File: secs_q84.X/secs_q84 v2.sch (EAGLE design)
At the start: 51 parts, among them IC1 MAX203ECWP, IC4 PIC18F47Q84-I_PT

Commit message: u[p
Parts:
- added SV2: CANBUS, con-lstb:MA06-1
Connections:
- net PVP_A renamed RS232_TX_OUT
- removed net PVP_B: A+REV.1, B-NORM.1, PVP_0.7
- new net RS232_RX_IN: A+REV.1, B-NORM.1, PVP_0.4
- net CANRX: now also SV2.2
- net CANTX: now also SV2.3
- net DERE: now also SV2.4
- net VCC: now also C2.1
- net VDD: now also SV2.5; no longer C2.1
- net VSS: now also SV2.1
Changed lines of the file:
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@@
 <part name="R1" library="rcl" library_urn="urn:adsk.eagle:library:334" deviceset="R-US_" device="R0805" package3d_urn="urn:adsk.eagle:package:23553/2" value="0ohm"/>
 <part name="VDD8" library="supply1" library_urn="urn:adsk.eagle:library:371" deviceset="VDD" device=""/>
+<part name="SV2" library="con-lstb" library_urn="urn:adsk.eagle:library:162" deviceset="MA06-1" device="" package3d_urn="urn:adsk.eagle:package:8340/1" value="CANBUS"/>
+<part name="P+4" library="supply1" library_urn="urn:adsk.eagle:library:371" deviceset="VCC" device=""/>
 </parts>
 <sheets>
@@
 </plain>
 <instances>
-<instance part="VDD1" gate="G$1" x="93.98" y="0" smashed="yes">
-<attribute name="VALUE" x="101.6" y="0" size="1.778" layer="96" rot="R180"/>
+<instance part="VDD1" gate="G$1" x="99.06" y="0" smashed="yes">
+<attribute name="VALUE" x="106.68" y="0" size="1.778" layer="96" rot="R180"/>
 </instance>
 <instance part="OS1_10MHZ" gate="A" x="134.62" y="-27.94" smashed="yes">
@@
 <attribute name="VALUE" x="46.99" y="-2.54" size="1.778" layer="96" align="center-left"/>
 </instance>
-<instance part="VSS47" gate="G$1" x="68.58" y="0" smashed="yes">
-<attribute name="VALUE" x="71.12" y="-5.08" size="1.778" layer="96" rot="R180"/>
+<instance part="VSS47" gate="G$1" x="71.12" y="2.54" smashed="yes" rot="R90">
+<attribute name="VALUE" x="73.66" y="2.54" size="1.778" layer="96"/>
 </instance>
 <instance part="VSS48" gate="G$1" x="71.12" y="5.08" smashed="yes" rot="R90">
-<attribute name="VALUE" x="76.2" y="7.62" size="1.778" layer="96" rot="R270"/>
+<attribute name="VALUE" x="73.66" y="5.08" size="1.778" layer="96"/>
 </instance>
 <instance part="R3" gate="G$1" x="223.52" y="114.3" smashed="yes" rot="R90">
@@
 <instance part="VDD8" gate="G$1" x="353.06" y="104.14" smashed="yes" rot="R270">
 <attribute name="VALUE" x="350.52" y="106.68" size="1.778" layer="96"/>
+</instance>
+<instance part="SV2" gate="1" x="307.34" y="-17.78" smashed="yes" rot="R180">
+<attribute name="VALUE" x="308.61" y="-5.08" size="1.778" layer="96" rot="R180"/>
+<attribute name="NAME" x="308.61" y="-26.162" size="1.778" layer="95" rot="R180"/>
+</instance>
+<instance part="P+4" gate="VCC" x="93.98" y="0" smashed="yes">
+<attribute name="VALUE" x="91.44" y="-2.54" size="1.778" layer="96" rot="R90"/>
 </instance>
 </instances>
@@
 <segment>
 <pinref part="VDD1" gate="G$1" pin="VDD"/>
-<wire x1="93.98" y1="-2.54" x2="99.06" y2="-2.54" width="0.1524" layer="91"/>
-<junction x="93.98" y="-2.54"/>
+<pinref part="C4" gate="G$1" pin="1"/>
 <junction x="99.06" y="-2.54"/>
-<pinref part="C2" gate="G$1" pin="1"/>
-<pinref part="C4" gate="G$1" pin="1"/>
 </segment>
 <segment>
@@
 <junction x="350.52" y="104.14"/>
 </segment>
+<segment>
+<wire x1="287.02" y1="-20.32" x2="299.72" y2="-20.32" width="0.1524" layer="91"/>
+<pinref part="SV2" gate="1" pin="5"/>
+<junction x="299.72" y="-20.32"/>
+<junction x="287.02" y="-20.32"/>
+<label x="289.56" y="-20.32" size="1.778" layer="95"/>
+</segment>
 </net>
 <net name="VSS" class="1">
@@
 <junction x="332.74" y="99.06"/>
 <junction x="345.44" y="99.06"/>
+</segment>
+<segment>
+<wire x1="287.02" y1="-10.16" x2="299.72" y2="-10.16" width="0.1524" layer="91"/>
+<pinref part="SV2" gate="1" pin="1"/>
+<junction x="299.72" y="-10.16"/>
+<junction x="287.02" y="-10.16"/>
+<label x="289.56" y="-10.16" size="1.778" layer="95"/>
 </segment>
 </net>
@@
 <label x="182.88" y="-20.32" size="1.778" layer="95"/>
 </segment>
+<segment>
+<wire x1="287.02" y1="-12.7" x2="299.72" y2="-12.7" width="0.1524" layer="91"/>
+<pinref part="SV2" gate="1" pin="2"/>
+<junction x="299.72" y="-12.7"/>
+<junction x="287.02" y="-12.7"/>
+<label x="289.56" y="-12.7" size="1.778" layer="95"/>
+</segment>
 </net>
 <net name="CANTX" class="0">
@@
 <label x="205.74" y="-66.04" size="1.778" layer="95" rot="R90"/>
 </segment>
+<segment>
+<wire x1="299.72" y1="-15.24" x2="287.02" y2="-15.24" width="0.1524" layer="91"/>
+<pinref part="SV2" gate="1" pin="3"/>
+<junction x="299.72" y="-15.24"/>
+<junction x="287.02" y="-15.24"/>
+<label x="289.56" y="-15.24" size="1.778" layer="95"/>
+</segment>
 </net>
 <net name="PC_TX2" class="0">
@@
 <junction x="220.98" y="25.4"/>
 <label x="220.98" y="15.24" size="1.778" layer="95" rot="R90"/>
+</segment>
+<segment>
+<wire x1="287.02" y1="-17.78" x2="299.72" y2="-17.78" width="0.1524" layer="91"/>
+<pinref part="SV2" gate="1" pin="4"/>
+<junction x="299.72" y="-17.78"/>
+<junction x="287.02" y="-17.78"/>
+<label x="289.56" y="-17.78" size="1.778" layer="95"/>
 </segment>
 </net>
@@
 </segment>
 </net>
-<net name="PVP_B" class="0">
+<net name="RS232_RX_IN" class="0">
 <segment>
 <pinref part="A+REV" gate="1" pin="1"/>
@@
 </segment>
 <segment>
-<wire x1="68.58" y1="10.16" x2="91.44" y2="10.16" width="0.1524" layer="91"/>
-<pinref part="PVP_0" gate="G$1" pin="7"/>
-<junction x="68.58" y="10.16"/>
-<junction x="91.44" y="10.16"/>
-<label x="81.28" y="10.16" size="1.778" layer="95"/>
-</segment>
-</net>
-<net name="PVP_A" class="0">
+<wire x1="22.86" y1="5.08" x2="45.72" y2="5.08" width="0.1524" layer="91"/>
+<pinref part="PVP_0" gate="G$1" pin="4"/>
+<label x="25.4" y="5.08" size="1.778" layer="95"/>
+<junction x="22.86" y="5.08"/>
+<junction x="45.72" y="5.08"/>
+</segment>
+</net>
+<net name="RS232_TX_OUT" class="0">
 <segment>
 <pinref part="A+NORM" gate="1" pin="1"/>
@@
 </segment>
 <segment>
-<wire x1="25.4" y1="2.54" x2="45.72" y2="2.54" width="0.1524" layer="91"/>
+<wire x1="22.86" y1="2.54" x2="45.72" y2="2.54" width="0.1524" layer="91"/>
 <pinref part="PVP_0" gate="G$1" pin="5"/>
 <junction x="45.72" y="2.54"/>
-<junction x="25.4" y="2.54"/>
-<label x="30.48" y="2.54" size="1.778" layer="95"/>
+<junction x="22.86" y="2.54"/>
+<label x="25.4" y="2.54" size="1.778" layer="95"/>
 </segment>
 </net>
@@
 <pinref part="P+3" gate="VCC" pin="VCC"/>
 <junction x="266.7" y="68.58"/>
+</segment>
+<segment>
+<pinref part="C2" gate="G$1" pin="1"/>
+<pinref part="P+4" gate="VCC" pin="VCC"/>
+<junction x="93.98" y="-2.54"/>
 </segment>
 </net>
@@
 </sheet>
 </sheets>
-<errors>
-</errors>
 </schematic>
 </drawing>

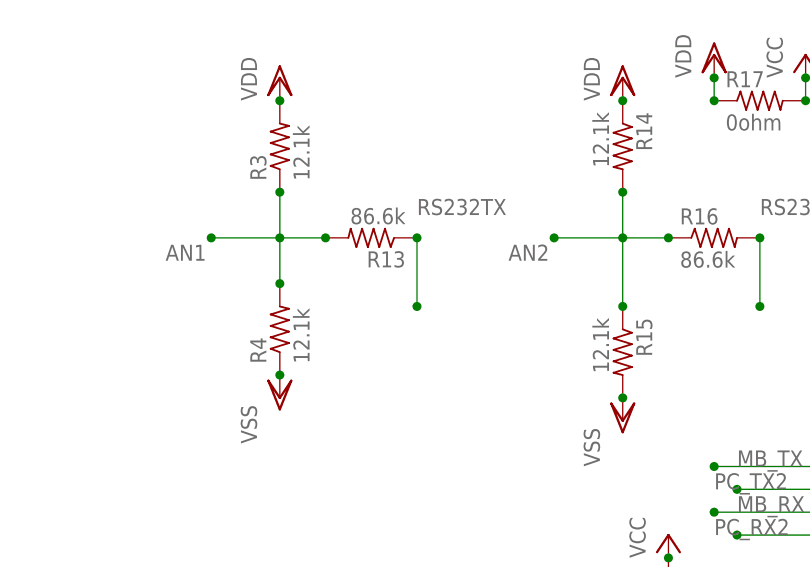
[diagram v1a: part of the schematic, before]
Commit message: two layer board
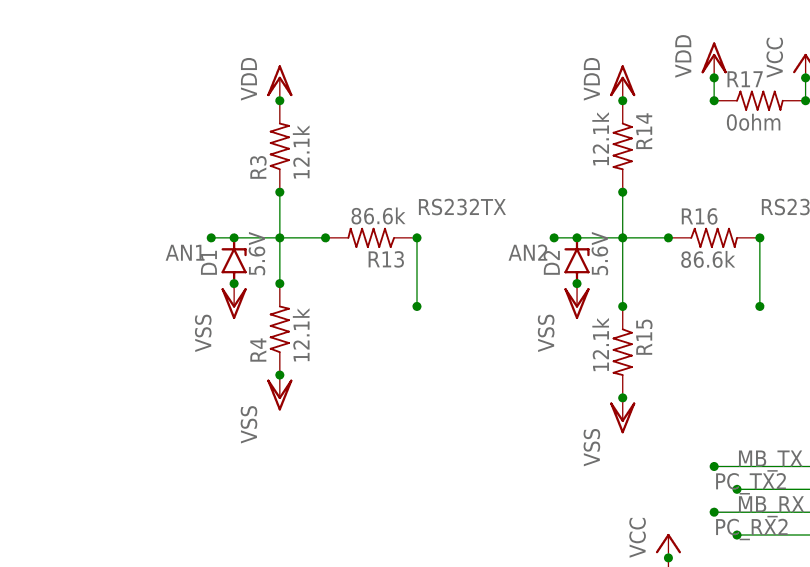
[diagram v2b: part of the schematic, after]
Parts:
- added D1, D2: 5.6V, diode:ZENER-DIODESMB
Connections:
- net AN1: now also D1.C
- net AN2: now also D2.C
- net VSS: now also D1.A, D2.A
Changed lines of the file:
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@@
 <part name="SV2" library="con-lstb" library_urn="urn:adsk.eagle:library:162" deviceset="MA06-1" device="" package3d_urn="urn:adsk.eagle:package:8340/1" value="CANBUS"/>
 <part name="P+4" library="supply1" library_urn="urn:adsk.eagle:library:371" deviceset="VCC" device=""/>
+<part name="D1" library="diode" library_urn="urn:adsk.eagle:library:210" deviceset="ZENER-DIODE" device="SMB" package3d_urn="urn:adsk.eagle:package:43404/2" value="5.6V"/>
+<part name="D2" library="diode" library_urn="urn:adsk.eagle:library:210" deviceset="ZENER-DIODE" device="SMB" package3d_urn="urn:adsk.eagle:package:43404/2" value="5.6V"/>
+<part name="VSS15" library="supply1" library_urn="urn:adsk.eagle:library:371" deviceset="VSS" device=""/>
+<part name="VSS16" library="supply1" library_urn="urn:adsk.eagle:library:371" deviceset="VSS" device=""/>
 </parts>
 <sheets>
@@
 <instance part="P+4" gate="VCC" x="93.98" y="0" smashed="yes">
 <attribute name="VALUE" x="91.44" y="-2.54" size="1.778" layer="96" rot="R90"/>
+</instance>
+<instance part="D1" gate="G$1" x="218.44" y="101.6" smashed="yes" rot="R90">
+<attribute name="NAME" x="216.535" y="99.822" size="1.778" layer="95" rot="R90"/>
+<attribute name="VALUE" x="221.869" y="99.822" size="1.778" layer="96" rot="R90"/>
+</instance>
+<instance part="D2" gate="G$1" x="256.54" y="101.6" smashed="yes" rot="R90">
+<attribute name="NAME" x="254.635" y="99.822" size="1.778" layer="95" rot="R90"/>
+<attribute name="VALUE" x="259.969" y="99.822" size="1.778" layer="96" rot="R90"/>
+</instance>
+<instance part="VSS15" gate="G$1" x="218.44" y="96.52" smashed="yes">
+<attribute name="VALUE" x="215.9" y="91.44" size="1.778" layer="96" rot="R90"/>
+</instance>
+<instance part="VSS16" gate="G$1" x="256.54" y="96.52" smashed="yes">
+<attribute name="VALUE" x="254" y="91.44" size="1.778" layer="96" rot="R90"/>
 </instance>
 </instances>
@@
 <label x="289.56" y="-10.16" size="1.778" layer="95"/>
 </segment>
+<segment>
+<pinref part="D1" gate="G$1" pin="A"/>
+<pinref part="VSS15" gate="G$1" pin="VSS"/>
+<junction x="218.44" y="99.06"/>
+</segment>
+<segment>
+<pinref part="D2" gate="G$1" pin="A"/>
+<pinref part="VSS16" gate="G$1" pin="VSS"/>
+<junction x="256.54" y="99.06"/>
+</segment>
 </net>
 <net name="CPU_CLK" class="0">
@@
 <wire x1="228.6" y1="104.14" x2="223.52" y2="104.14" width="0.1524" layer="91"/>
 <junction x="223.52" y="104.14"/>
-<wire x1="223.52" y1="104.14" x2="215.9" y2="104.14" width="0.1524" layer="91"/>
+<wire x1="223.52" y1="104.14" x2="218.44" y2="104.14" width="0.1524" layer="91"/>
 <junction x="228.6" y="104.14"/>
 <junction x="215.9" y="104.14"/>
@@
 <junction x="223.52" y="109.22"/>
 <label x="210.82" y="101.6" size="1.778" layer="95"/>
+<pinref part="D1" gate="G$1" pin="C"/>
+<wire x1="218.44" y1="104.14" x2="215.9" y2="104.14" width="0.1524" layer="91"/>
+<junction x="218.44" y="104.14"/>
 </segment>
 </net>
@@
 <wire x1="266.7" y1="104.14" x2="261.62" y2="104.14" width="0.1524" layer="91"/>
 <junction x="261.62" y="104.14"/>
-<wire x1="261.62" y1="104.14" x2="254" y2="104.14" width="0.1524" layer="91"/>
+<wire x1="261.62" y1="104.14" x2="256.54" y2="104.14" width="0.1524" layer="91"/>
 <junction x="266.7" y="104.14"/>
 <junction x="254" y="104.14"/>
@@
 <junction x="261.62" y="96.52"/>
 <label x="248.92" y="101.6" size="1.778" layer="95"/>
-</segment>
-</net>
+<pinref part="D2" gate="G$1" pin="C"/>
+<wire x1="256.54" y1="104.14" x2="254" y2="104.14" width="0.1524" layer="91"/>
+<junction x="256.54" y="104.14"/>
+</segment>
+</net>

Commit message: up
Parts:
- added F1: 0805L075WR, 0805L075WR:0805L075WR
- added GLORY: GLORY, pinhead:PINHD-1X2
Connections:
- new net POWERIN: F1.1, GLORY.2
- net VDD: now also F1.2
- net VSS: now also GLORY.1
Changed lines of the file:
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@@
 <part name="VSS15" library="supply1" library_urn="urn:adsk.eagle:library:371" deviceset="VSS" device=""/>
 <part name="VSS16" library="supply1" library_urn="urn:adsk.eagle:library:371" deviceset="VSS" device=""/>
+<part name="GLORY" library="pinhead" library_urn="urn:adsk.eagle:library:325" deviceset="PINHD-1X2" device="" package3d_urn="urn:adsk.eagle:package:22435/2" value="GLORY"/>
+<part name="VSS17" library="supply1" library_urn="urn:adsk.eagle:library:371" deviceset="VSS" device=""/>
+<part name="VDD10" library="supply1" library_urn="urn:adsk.eagle:library:371" deviceset="VDD" device=""/>
+<part name="F1" library="0805L075WR" deviceset="0805L075WR" device=""/>
 </parts>
 <sheets>
@@
 <instance part="VSS16" gate="G$1" x="256.54" y="96.52" smashed="yes">
 <attribute name="VALUE" x="254" y="91.44" size="1.778" layer="96" rot="R90"/>
+</instance>
+<instance part="GLORY" gate="G$1" x="83.82" y="88.9" smashed="yes" rot="R180">
+<attribute name="NAME" x="90.17" y="83.185" size="1.778" layer="95" rot="R180"/>
+<attribute name="VALUE" x="80.01" y="88.9" size="1.778" layer="96" rot="R180"/>
+</instance>
+<instance part="VSS17" gate="G$1" x="101.6" y="83.82" smashed="yes">
+<attribute name="VALUE" x="104.14" y="81.28" size="1.778" layer="96" rot="R180"/>
+</instance>
+<instance part="VDD10" gate="G$1" x="111.76" y="91.44" smashed="yes">
+<attribute name="VALUE" x="114.3" y="96.52" size="1.778" layer="96" rot="R180"/>
+</instance>
+<instance part="F1" gate="G$1" x="93.98" y="88.9" smashed="yes">
+<attribute name="NAME" x="90.17" y="95.25" size="1.778" layer="95" align="center-left"/>
+<attribute name="VALUE" x="95.25" y="95.25" size="1.778" layer="96" align="center-left"/>
 </instance>
 </instances>
@@
 <label x="289.56" y="-20.32" size="1.778" layer="95"/>
 </segment>
+<segment>
+<pinref part="F1" gate="G$1" pin="2"/>
+<pinref part="VDD10" gate="G$1" pin="VDD"/>
+<junction x="111.76" y="88.9"/>
+</segment>
 </net>
 <net name="VSS" class="1">
@@
 <pinref part="VSS16" gate="G$1" pin="VSS"/>
 <junction x="256.54" y="99.06"/>
+</segment>
+<segment>
+<pinref part="GLORY" gate="G$1" pin="1"/>
+<wire x1="86.36" y1="86.36" x2="101.6" y2="86.36" width="0.1524" layer="91"/>
+<pinref part="VSS17" gate="G$1" pin="VSS"/>
+<junction x="86.36" y="86.36"/>
+<junction x="101.6" y="86.36"/>
 </segment>
 </net>
@@
 </segment>
 </net>
+<net name="POWERIN" class="1">
+<segment>
+<pinref part="GLORY" gate="G$1" pin="2"/>
+<pinref part="F1" gate="G$1" pin="1"/>
+<wire x1="86.36" y1="88.9" x2="93.98" y2="88.9" width="0.1524" layer="91"/>
+<junction x="93.98" y="88.9"/>
+<junction x="86.36" y="88.9"/>
+<label x="76.2" y="93.98" size="1.778" layer="95"/>
+</segment>
+</net>

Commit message: up
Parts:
- renumbered OS1_10MHZ to OS1_16MHZ
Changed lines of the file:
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@@
 <parts>
 <part name="VDD1" library="supply1" library_urn="urn:adsk.eagle:library:371" deviceset="VDD" device=""/>
-<part name="OS1_10MHZ" library="IQD-Frequency-Products" library_urn="urn:adsk.eagle:library:90" deviceset="OSC-OE" device="-CFPS-72" package3d_urn="urn:adsk.eagle:package:3365/1"/>
+<part name="OS1_16MHZ" library="IQD-Frequency-Products" library_urn="urn:adsk.eagle:library:90" deviceset="OSC-OE" device="-CFPS-72" package3d_urn="urn:adsk.eagle:package:3365/1"/>
 <part name="VDD3" library="supply1" library_urn="urn:adsk.eagle:library:371" deviceset="VDD" device=""/>
 <part name="VSS4" library="supply1" library_urn="urn:adsk.eagle:library:371" deviceset="VSS" device=""/>
@@
 <attribute name="VALUE" x="106.68" y="0" size="1.778" layer="96" rot="R180"/>
 </instance>
-<instance part="OS1_10MHZ" gate="A" x="134.62" y="-27.94" smashed="yes">
+<instance part="OS1_16MHZ" gate="A" x="134.62" y="-27.94" smashed="yes">
 <attribute name="NAME" x="127" y="-19.685" size="1.778" layer="95"/>
 <attribute name="VALUE" x="127" y="-38.1" size="1.778" layer="96"/>
@@
 </segment>
 <segment>
-<pinref part="OS1_10MHZ" gate="A" pin="VDD"/>
+<pinref part="OS1_16MHZ" gate="A" pin="VDD"/>
 <pinref part="VDD3" gate="G$1" pin="VDD"/>
 <junction x="121.92" y="-22.86"/>
@@
 </segment>
 <segment>
-<pinref part="OS1_10MHZ" gate="A" pin="CON"/>
+<pinref part="OS1_16MHZ" gate="A" pin="CON"/>
 <pinref part="VDD4" gate="G$1" pin="VDD"/>
 <junction x="147.32" y="-22.86"/>
@@
 </segment>
 <segment>
-<pinref part="OS1_10MHZ" gate="A" pin="VSS"/>
+<pinref part="OS1_16MHZ" gate="A" pin="VSS"/>
 <pinref part="VSS4" gate="G$1" pin="VSS"/>
 <junction x="121.92" y="-33.02"/>
@@
 <net name="CPU_CLK" class="0">
 <segment>
-<pinref part="OS1_10MHZ" gate="A" pin="OUT"/>
+<pinref part="OS1_16MHZ" gate="A" pin="OUT"/>
 <wire x1="147.32" y1="-27.94" x2="157.48" y2="-27.94" width="0.1524" layer="91"/>
 <label x="149.86" y="-33.02" size="1.778" layer="95"/>
